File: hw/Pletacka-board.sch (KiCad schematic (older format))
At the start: 3 parts, among them J4 Conn_01x02_Female, J5 Conn_01x03_Female

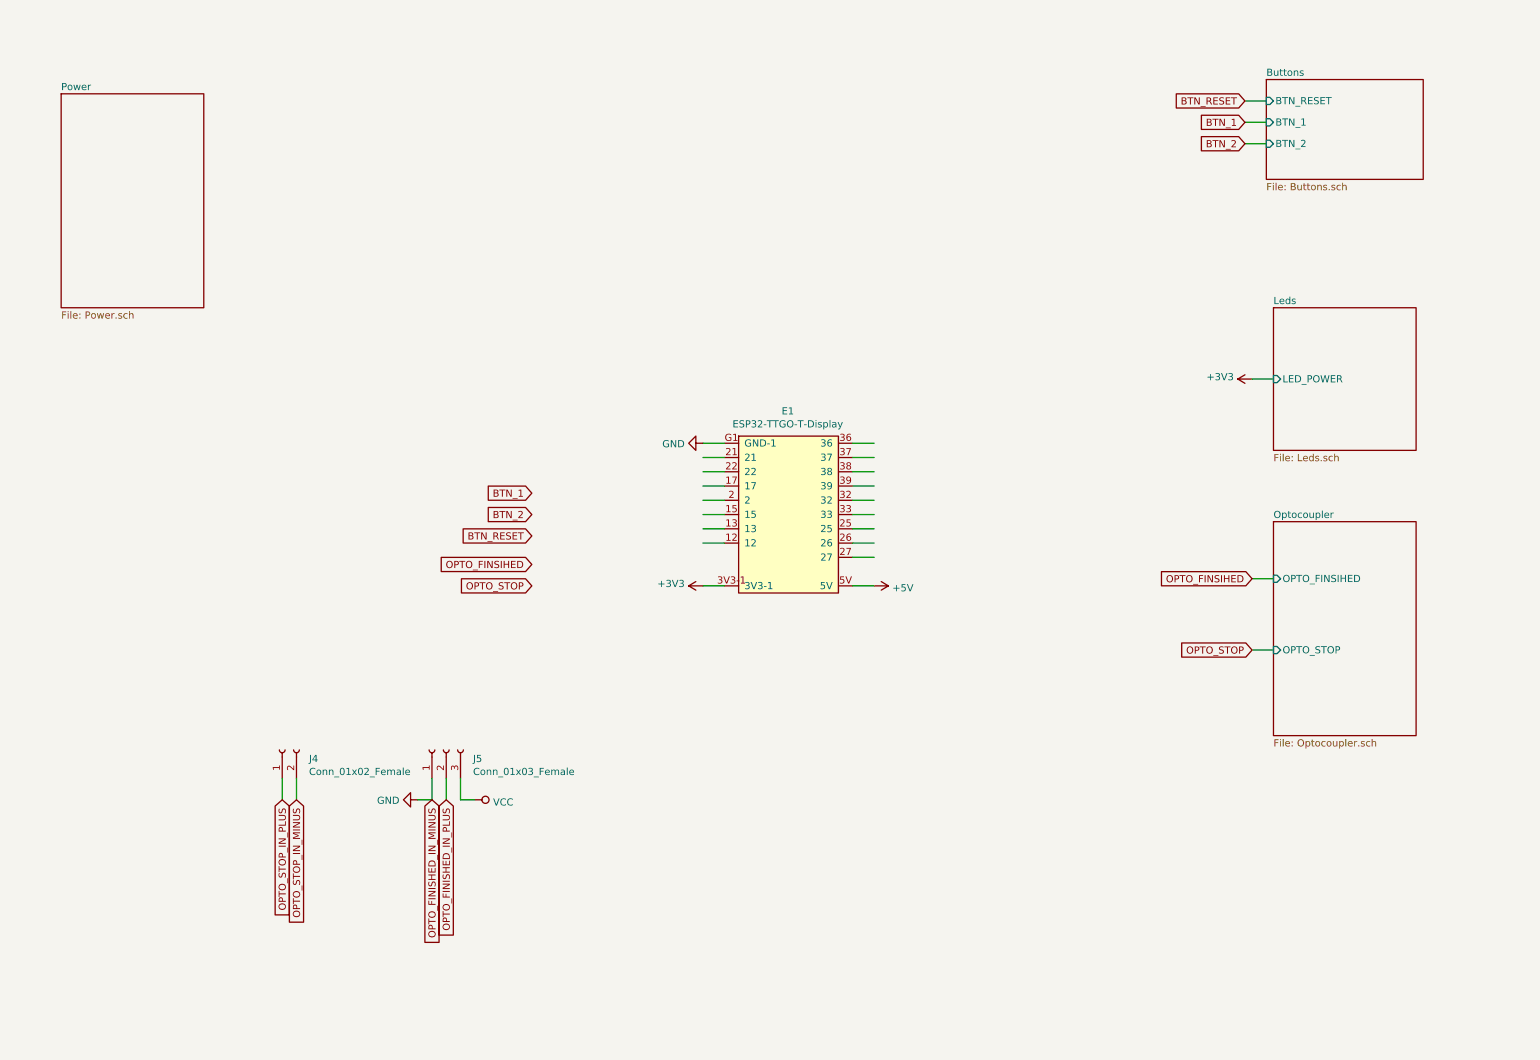
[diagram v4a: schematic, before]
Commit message: Update some packages, add 3D models
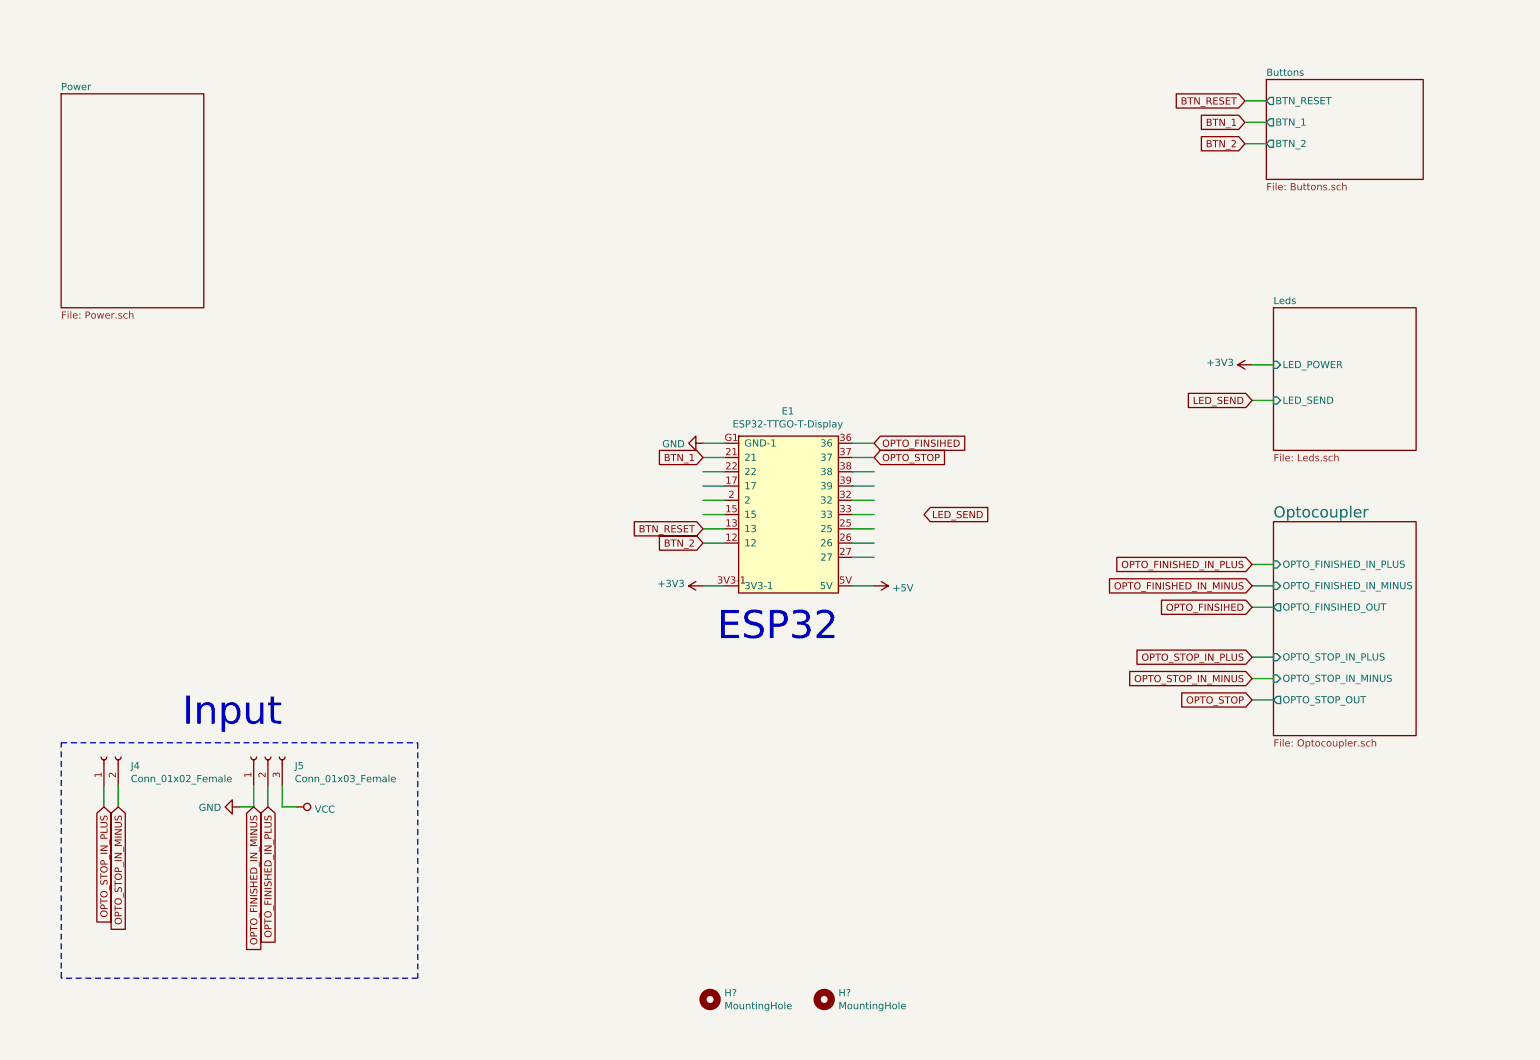
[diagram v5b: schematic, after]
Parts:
- added H? (x2): MountingHole, symbol Mechanical:MountingHole
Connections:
- net labels added: LED_SEND
- wire segments 32 -> 37
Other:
- note added: "ESP32"
- note added: "Input"
- moved on the sheet: J4, J5
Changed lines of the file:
@@
 F0 "Buttons" 50
 F1 "Buttons.sch" 50
-F2 "BTN_RESET" I L 9450 1050 50
-F3 "BTN_1" I L 9450 1200 50
-F4 "BTN_2" I L 9450 1350 50
+F2 "BTN_RESET" O L 9450 1050 50
+F3 "BTN_1" O L 9450 1200 50
+F4 "BTN_2" O L 9450 1350 50
 $EndSheet
 Text GLabel 9300 1050 0    50   Input ~ 0
@@
 Wire Wire Line
 	9300 1350 9450 1350
-Text GLabel 4300 3800 0    50   Input ~ 0
+Text GLabel 5500 3550 0    50   Input ~ 0
 BTN_1
-Text GLabel 4300 3950 0    50   Input ~ 0
+Text GLabel 5500 4150 0    50   Input ~ 0
 BTN_2
-Text GLabel 4300 4100 0    50   Input ~ 0
+Text GLabel 5500 4050 0    50   Input ~ 0
 BTN_RESET
 Wire Wire Line
@@
 F0 "Leds" 50
 F1 "Leds.sch" 50
-F2 "LED_POWER" I L 9500 3000 50
-$EndSheet
-Wire Wire Line
-	9350 3000 9500 3000
+F2 "LED_POWER" I L 9500 2900 50
+F3 "LED_SEND" I L 9500 3150 50
+$EndSheet
 $Comp
 L power:+3V3 #PWR0104
 U 1 1 5F8DEB09
-P 9350 3000
-F 0 "#PWR0104" H 9350 2850 50  0001 C CNN
-F 1 "+3V3" V 9365 3128 50  0000 L CNN
-F 2 "" H 9350 3000 50  0001 C CNN
-F 3 "" H 9350 3000 50  0001 C CNN
-	1    9350 3000
+P 9350 2900
+F 0 "#PWR0104" H 9350 2750 50  0001 C CNN
+F 1 "+3V3" V 9365 3028 50  0000 L CNN
+F 2 "" H 9350 2900 50  0001 C CNN
+F 3 "" H 9350 2900 50  0001 C CNN
+	1    9350 2900
 	0    -1   -1   0
 $EndComp
@@
 S 9500 4000 1000 1500
 U 5F8B0B95
-F0 "Optocoupler" 50
+F0 "Optocoupler" 79
 F1 "Optocoupler.sch" 50
-F2 "OPTO_FINSIHED" I L 9500 4400 50
-F3 "OPTO_STOP" I L 9500 4900 50
-$EndSheet
-Text GLabel 9350 4400 0    50   Input ~ 0
+F2 "OPTO_FINSIHED_OUT" O L 9500 4600 50
+F3 "OPTO_STOP_OUT" O L 9500 5250 50
+F4 "OPTO_STOP_IN_PLUS" I L 9500 4950 50
+F5 "OPTO_STOP_IN_MINUS" I L 9500 5100 50
+F6 "OPTO_FINISHED_IN_MINUS" I L 9500 4450 50
+F7 "OPTO_FINISHED_IN_PLUS" I L 9500 4300 50
+$EndSheet
+Text GLabel 9350 4600 0    50   Input ~ 0
 OPTO_FINSIHED
-Text GLabel 9350 4900 0    50   Input ~ 0
+Text GLabel 9350 5250 0    50   Input ~ 0
 OPTO_STOP
 Wire Wire Line
-	9350 4400 9500 4400
-Wire Wire Line
-	9500 4900 9350 4900
-Text GLabel 4300 4300 0    50   Input ~ 0
+	9500 5250 9350 5250
+Text GLabel 6700 3450 2    50   Input ~ 0
 OPTO_FINSIHED
-Text GLabel 4300 4450 0    50   Input ~ 0
+Text GLabel 6700 3550 2    50   Input ~ 0
 OPTO_STOP
 $Sheet
@@
 L Connector:Conn_01x02_Female J4
 U 1 1 5F9151EB
-P 2550 5600
-F 0 "J4" V 2488 5412 50  0000 R CNN
-F 1 "Conn_01x02_Female" V 2397 5412 50  0000 R CNN
-F 2 "Terminal_block:TerminalBlock_Phoenix_PT-1,5-2-5.0-H_1x02_P5.00mm_Horizontal" H 2550 5600 50  0001 C CNN
-F 3 "~" H 2550 5600 50  0001 C CNN
-	1    2550 5600
+P 1300 5650
+F 0 "J4" V 1238 5462 50  0000 R CNN
+F 1 "Conn_01x02_Female" V 1147 5462 50  0000 R CNN
+F 2 "Terminal_block:TerminalBlock_Phoenix_PT-1,5-2-5.0-H_1x02_P5.00mm_Horizontal" H 1300 5650 50  0001 C CNN
+F 3 "~" H 1300 5650 50  0001 C CNN
+	1    1300 5650
 	0    -1   -1   0
 $EndComp
@@
 L Connector:Conn_01x03_Female J5
 U 1 1 5F915FED
-P 3700 5600
-F 0 "J5" V 3638 5412 50  0000 R CNN
-F 1 "Conn_01x03_Female" V 3547 5412 50  0000 R CNN
-F 2 "Terminal_block:TerminalBlock_Phoenix_PT-1,5-3-5.0-H_1x03_P5.00mm_Horizontal" H 3700 5600 50  0001 C CNN
-F 3 "~" H 3700 5600 50  0001 C CNN
-	1    3700 5600
+P 2450 5650
+F 0 "J5" V 2388 5462 50  0000 R CNN
+F 1 "Conn_01x03_Female" V 2297 5462 50  0000 R CNN
+F 2 "Terminal_block:TerminalBlock_Phoenix_PT-1,5-3-5.0-H_1x03_P5.00mm_Horizontal" H 2450 5650 50  0001 C CNN
+F 3 "~" H 2450 5650 50  0001 C CNN
+	1    2450 5650
 	0    -1   -1   0
 $EndComp
 Wire Wire Line
-	2550 5950 2550 5800
-Wire Wire Line
-	2650 5950 2650 5800
-Wire Wire Line
-	3600 5950 3600 5800
-Wire Wire Line
-	3700 5950 3700 5800
-Wire Wire Line
-	3800 5950 3800 5800
-Text GLabel 2550 5950 3    50   Input ~ 0
+	1300 6000 1300 5850
+Wire Wire Line
+	1400 6000 1400 5850
+Wire Wire Line
+	2350 6000 2350 5850
+Wire Wire Line
+	2450 6000 2450 5850
+Wire Wire Line
+	2550 6000 2550 5850
+Text GLabel 1300 6000 3    50   Input ~ 0
 OPTO_STOP_IN_PLUS
-Text GLabel 2650 5950 3    50   Input ~ 0
+Text GLabel 1400 6000 3    50   Input ~ 0
 OPTO_STOP_IN_MINUS
-Text GLabel 3600 5950 3    50   Input ~ 0
+Text GLabel 2350 6000 3    50   Input ~ 0
 OPTO_FINISHED_IN_MINUS
-Text GLabel 3700 5950 3    50   Input ~ 0
+Text GLabel 2450 6000 3    50   Input ~ 0
 OPTO_FINISHED_IN_PLUS
 Wire Wire Line
-	3800 5950 3900 5950
-Wire Wire Line
-	3600 5950 3500 5950
+	2550 6000 2650 6000
+Wire Wire Line
+	2350 6000 2250 6000
 $Comp
 L power:GND #PWR0116
 U 1 1 5F91B916
-P 3500 5950
-F 0 "#PWR0116" H 3500 5700 50  0001 C CNN
-F 1 "GND" V 3505 5822 50  0000 R CNN
-F 2 "" H 3500 5950 50  0001 C CNN
-F 3 "" H 3500 5950 50  0001 C CNN
-	1    3500 5950
+P 2250 6000
+F 0 "#PWR0116" H 2250 5750 50  0001 C CNN
+F 1 "GND" V 2255 5872 50  0000 R CNN
+F 2 "" H 2250 6000 50  0001 C CNN
+F 3 "" H 2250 6000 50  0001 C CNN
+	1    2250 6000
 	0    1    1    0
 $EndComp
@@
 L power:VCC #PWR0117
 U 1 1 5F91BD5C
-P 3900 5950
-F 0 "#PWR0117" H 3900 5800 50  0001 C CNN
-F 1 "VCC" V 3917 6078 50  0000 L CNN
-F 2 "" H 3900 5950 50  0001 C CNN
-F 3 "" H 3900 5950 50  0001 C CNN
-	1    3900 5950
+P 2650 6000
+F 0 "#PWR0117" H 2650 5850 50  0001 C CNN
+F 1 "VCC" V 2667 6128 50  0000 L CNN
+F 2 "" H 2650 6000 50  0001 C CNN
+F 3 "" H 2650 6000 50  0001 C CNN
+	1    2650 6000
 	0    1    1    0
 $EndComp
+Text GLabel 9350 4950 0    50   Input ~ 0
+OPTO_STOP_IN_PLUS
+Text GLabel 9350 5100 0    50   Input ~ 0
+OPTO_STOP_IN_MINUS
+Wire Wire Line
+	9350 5100 9500 5100
+Wire Wire Line
+	9350 4950 9500 4950
+Wire Wire Line
+	9350 4600 9500 4600
+Text GLabel 9350 4300 0    50   Input ~ 0
+OPTO_FINISHED_IN_PLUS
+Text GLabel 9350 4450 0    50   Input ~ 0
+OPTO_FINISHED_IN_MINUS
+Wire Wire Line
+	9350 4450 9500 4450
+Wire Wire Line
+	9500 4300 9350 4300
+Text Notes 5600 4850 0    197  ~ 0
+ESP32
+Wire Notes Line
+	1000 5550 3500 5550
+Wire Notes Line
+	3500 5550 3500 7200
+Wire Notes Line
+	3500 7200 1000 7200
+Wire Notes Line
+	1000 7200 1000 5550
+Text Notes 1850 5450 0    197  ~ 0
+Input
+Wire Wire Line
+	9350 2900 9500 2900
+Wire Wire Line
+	9500 3150 9350 3150
+Text GLabel 9350 3150 0    50   Input ~ 0
+LED_SEND
+Text GLabel 7050 3950 2    50   Input ~ 0
+LED_SEND
+$Comp
+L Mechanical:MountingHole H?
+U 1 1 5F9A015D
+P 6350 7350
+F 0 "H?" H 6450 7396 50  0000 L CNN
+F 1 "MountingHole" H 6450 7305 50  0000 L CNN
+F 2 "" H 6350 7350 50  0001 C CNN
+F 3 "~" H 6350 7350 50  0001 C CNN
+	1    6350 7350
+	1    0    0    -1
+$EndComp
+$Comp
+L Mechanical:MountingHole H?
+U 1 1 5F9A042D
+P 5550 7350
+F 0 "H?" H 5650 7396 50  0000 L CNN
+F 1 "MountingHole" H 5650 7305 50  0000 L CNN
+F 2 "" H 5550 7350 50  0001 C CNN
+F 3 "~" H 5550 7350 50  0001 C CNN
+	1    5550 7350
+	1    0    0    -1
+$EndComp
 $EndSCHEMATC

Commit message: Routing schema
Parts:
- H1, H2: renamed from H?; footprint (none) -> MountingHole:MountingHole_2.7mm_M2.5_Pad
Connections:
- net labels removed: BTN_2, OPTO_FINISHED_IN_MINUS
- wire segments 37 -> 36
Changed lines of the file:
@@
 F2 "BTN_RESET" O L 9450 1050 50
 F3 "BTN_1" O L 9450 1200 50
-F4 "BTN_2" O L 9450 1350 50
 $EndSheet
 Text GLabel 9300 1050 0    50   Input ~ 0
@@
 Text GLabel 9300 1200 0    50   Input ~ 0
 BTN_1
-Text GLabel 9300 1350 0    50   Input ~ 0
-BTN_2
 Wire Wire Line
 	9450 1200 9300 1200
-Wire Wire Line
-	9300 1350 9450 1350
 Text GLabel 5500 3550 0    50   Input ~ 0
 BTN_1
-Text GLabel 5500 4150 0    50   Input ~ 0
-BTN_2
 Text GLabel 5500 4050 0    50   Input ~ 0
 BTN_RESET
@@
 Text GLabel 1400 6000 3    50   Input ~ 0
 OPTO_STOP_IN_MINUS
-Text GLabel 2350 6000 3    50   Input ~ 0
-OPTO_FINISHED_IN_MINUS
 Text GLabel 2450 6000 3    50   Input ~ 0
 OPTO_FINISHED_IN_PLUS
@@
 Text GLabel 9350 4300 0    50   Input ~ 0
 OPTO_FINISHED_IN_PLUS
-Text GLabel 9350 4450 0    50   Input ~ 0
-OPTO_FINISHED_IN_MINUS
 Wire Wire Line
 	9350 4450 9500 4450
@@
 LED_SEND
 $Comp
-L Mechanical:MountingHole H?
+L Mechanical:MountingHole H2
 U 1 1 5F9A015D
 P 6350 7350
-F 0 "H?" H 6450 7396 50  0000 L CNN
+F 0 "H2" H 6450 7396 50  0000 L CNN
 F 1 "MountingHole" H 6450 7305 50  0000 L CNN
-F 2 "" H 6350 7350 50  0001 C CNN
+F 2 "MountingHole:MountingHole_2.7mm_M2.5_Pad" H 6350 7350 50  0001 C CNN
 F 3 "~" H 6350 7350 50  0001 C CNN
 	1    6350 7350
@@
 $EndComp
 $Comp
-L Mechanical:MountingHole H?
+L Mechanical:MountingHole H1
 U 1 1 5F9A042D
 P 5550 7350
-F 0 "H?" H 5650 7396 50  0000 L CNN
+F 0 "H1" H 5650 7396 50  0000 L CNN
 F 1 "MountingHole" H 5650 7305 50  0000 L CNN
-F 2 "" H 5550 7350 50  0001 C CNN
+F 2 "MountingHole:MountingHole_2.7mm_M2.5_Pad" H 5550 7350 50  0001 C CNN
 F 3 "~" H 5550 7350 50  0001 C CNN
 	1    5550 7350
 	1    0    0    -1
 $EndComp
+$Comp
+L power:GND #PWR0107
+U 1 1 5F9CF981
+P 9350 4450
+F 0 "#PWR0107" H 9350 4200 50  0001 C CNN
+F 1 "GND" V 9355 4322 50  0000 R CNN
+F 2 "" H 9350 4450 50  0001 C CNN
+F 3 "" H 9350 4450 50  0001 C CNN
+	1    9350 4450
+	0    1    1    0
+$EndComp
 $EndSCHEMATC

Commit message: Routing board
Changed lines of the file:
@@
 Text GLabel 9350 3150 0    50   Input ~ 0
 LED_SEND
-Text GLabel 7050 3950 2    50   Input ~ 0
+Text GLabel 6700 4050 2    50   Input ~ 0
 LED_SEND
 $Comp

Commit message: Update improve schema and broke board
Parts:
- removed H2: MountingHole, MountingHole:MountingHole_2.7mm_M2.5_Pad, symbol Mechanical:MountingHole
- added C? (x3): 100n, Capacitor_SMD:C_0603_1608Metric, symbol Device:C
- added C?: 10u/50V, Capacitor_SMD:C_1206_3216Metric, symbol Device:C
- added C?: 8.2n, Capacitor_SMD:C_0603_1608Metric, symbol Device:C
- added C?: 22n, Capacitor_SMD:C_0603_1608Metric, symbol Device:C
- added C?: 33n, Capacitor_SMD:C_0603_1608Metric, symbol Device:C
- added C?: 22u, Capacitor_SMD:C_0603_1608Metric, symbol Device:C
- added D? (x2): LED, LED_SMD:LED_0603_1608Metric, symbol Device:LED
- added D? (x2): B5819W, B5819W:B5819W_SOD-123, symbol B5819W:B5819W
- added D?: 1SMB5935BT3G, 1SMB5935BT3G:DIOM5436X247N, symbol 1SMB5935BT3G:1SMB5935BT3G
- added D? (x2): SS34, SS34:SMA, symbol SS34:SS34
- added L?: L, Inductor_SMD:L_TDK_SLF7045, symbol Device:L
- added POLYFUSE?: 24V 1A, Resistor_SMD:R_1206_3216Metric, symbol Device:R
- added R? (x4): 2k2, Resistor_SMD:R_0603_1608Metric, symbol Device:R
- added R? (x2): 20k, Resistor_SMD:R_0603_1608Metric, symbol Device:R
- added R? (x2): 10k, Resistor_SMD:R_0603_1608Metric, symbol Device:R
- added R?: 100-OH, Resistor_SMD:R_0603_1608Metric, symbol Device:R
- added R?: 4k7, Resistor_SMD:R_0603_1608Metric, symbol Device:R
- added R?: 15k, Resistor_SMD:R_0603_1608Metric, symbol Device:R
- added SW?: Reset_Button, Button_SMD:SW_SPST_SKQG_WithStem, symbol Switch:SW_Push_Dual_x2
- added SW?: User_Button, Button_SMD:SW_SPST_SKQG_WithStem, symbol Switch:SW_Push_Dual_x2
- added U? (x2): EL357N(A)(TA)-G, EL357N_A__TA_-G:SOP254P700X200-4N, symbol EL357N_A__TA_-G:EL357N(A)(TA)-G
- added U?: TPS54231D, SOIC127P599X175-8N, symbol TPS54231D:TPS54231D
- J4: value Conn_01x02_Female -> STOP_INPUT
- J5: value Conn_01x03_Female -> POWER_&_FINN_INPUT
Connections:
- net labels added: LED_USER
- net labels removed: LED_SEND
- wire segments 36 -> 129
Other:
- note added: "Buttons"
- note added: "LEDs"
- note added: "Optocoupler FINISHED"
- note added: "Optocoupler STOP"
- note added: "Optocouplers"
- note added: "Pletacka board v2.0"
- note added: "Power"
- note added: "Power LED"
- note added: "Reset button"
- note added: "User LED"
- note added: "User button"
- moved on the sheet: E1, H1
